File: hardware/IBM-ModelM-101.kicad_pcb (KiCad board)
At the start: 2 copper layers, 150 x 50 mm, 40 parts, among them J1 CONN-61729-USB-B, J2 KEYBOARD_ACTIVE_LINES, J3 KEYBOARD_INPUT_LINES, J4 CHASSIS_GROUND, J5 STATUS_LEDS, J6 DEBUG_FTDI, J7 JTAG, SW1 TACT-TE-FSMSM, SW2 TACT-TE-FSMSM, U1 TLV70233DBV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

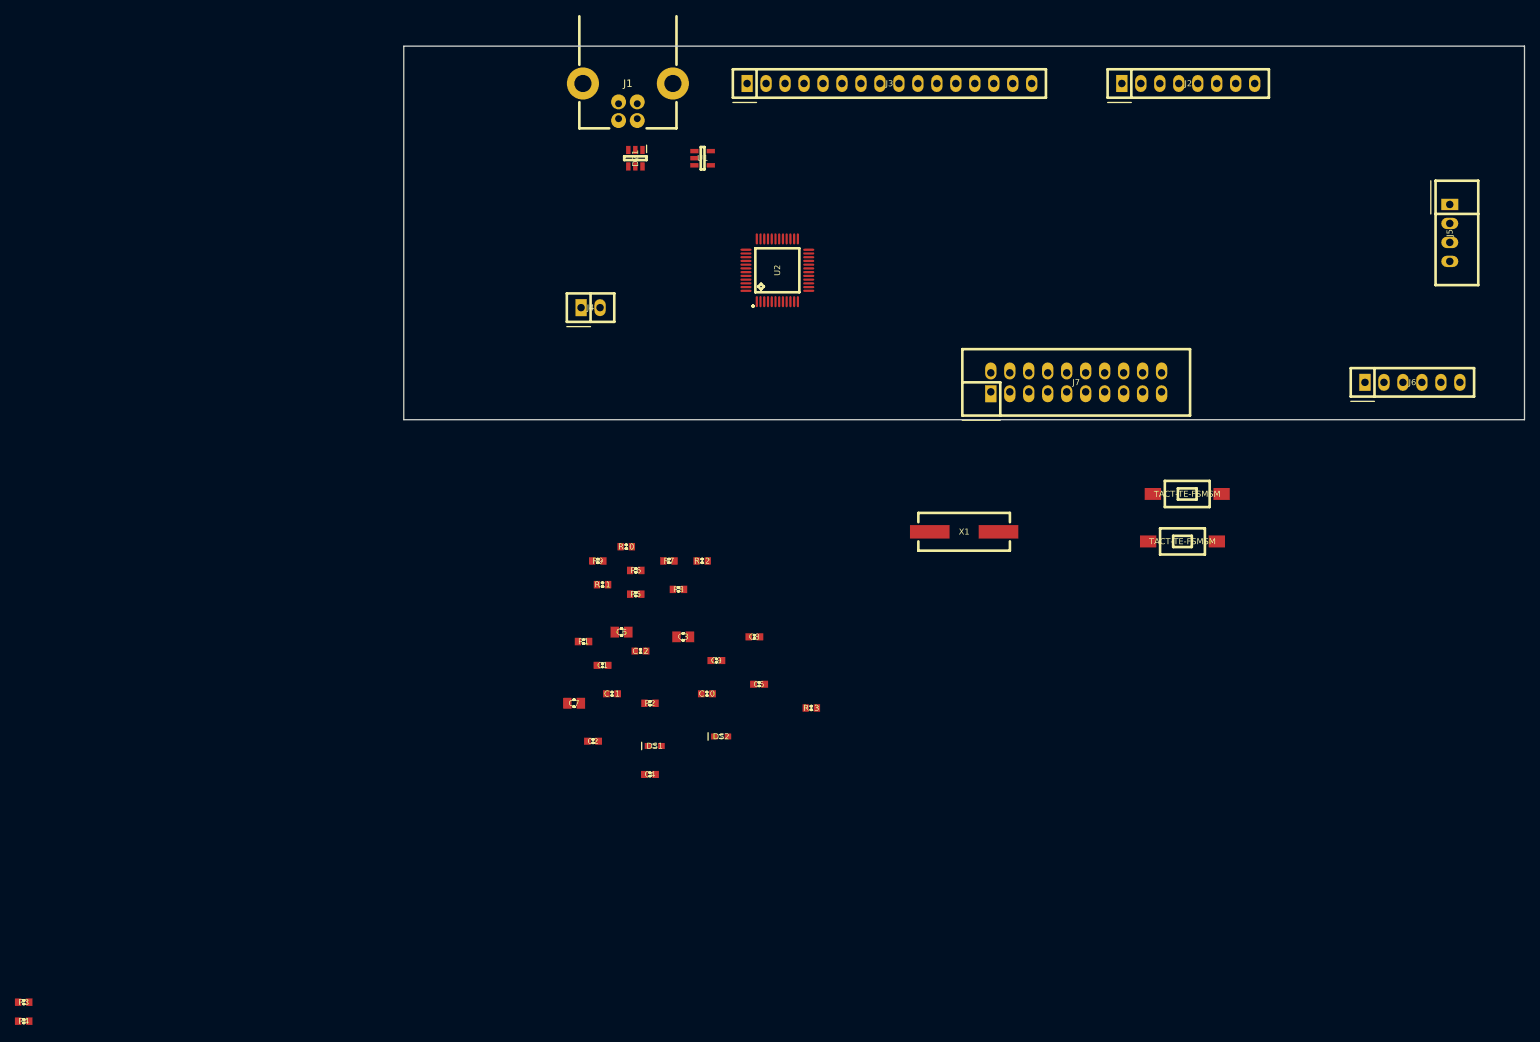
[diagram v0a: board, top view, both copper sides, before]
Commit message: Working on PCB layout
Placement is done. Most of the power, decoupling and support routing
finished.
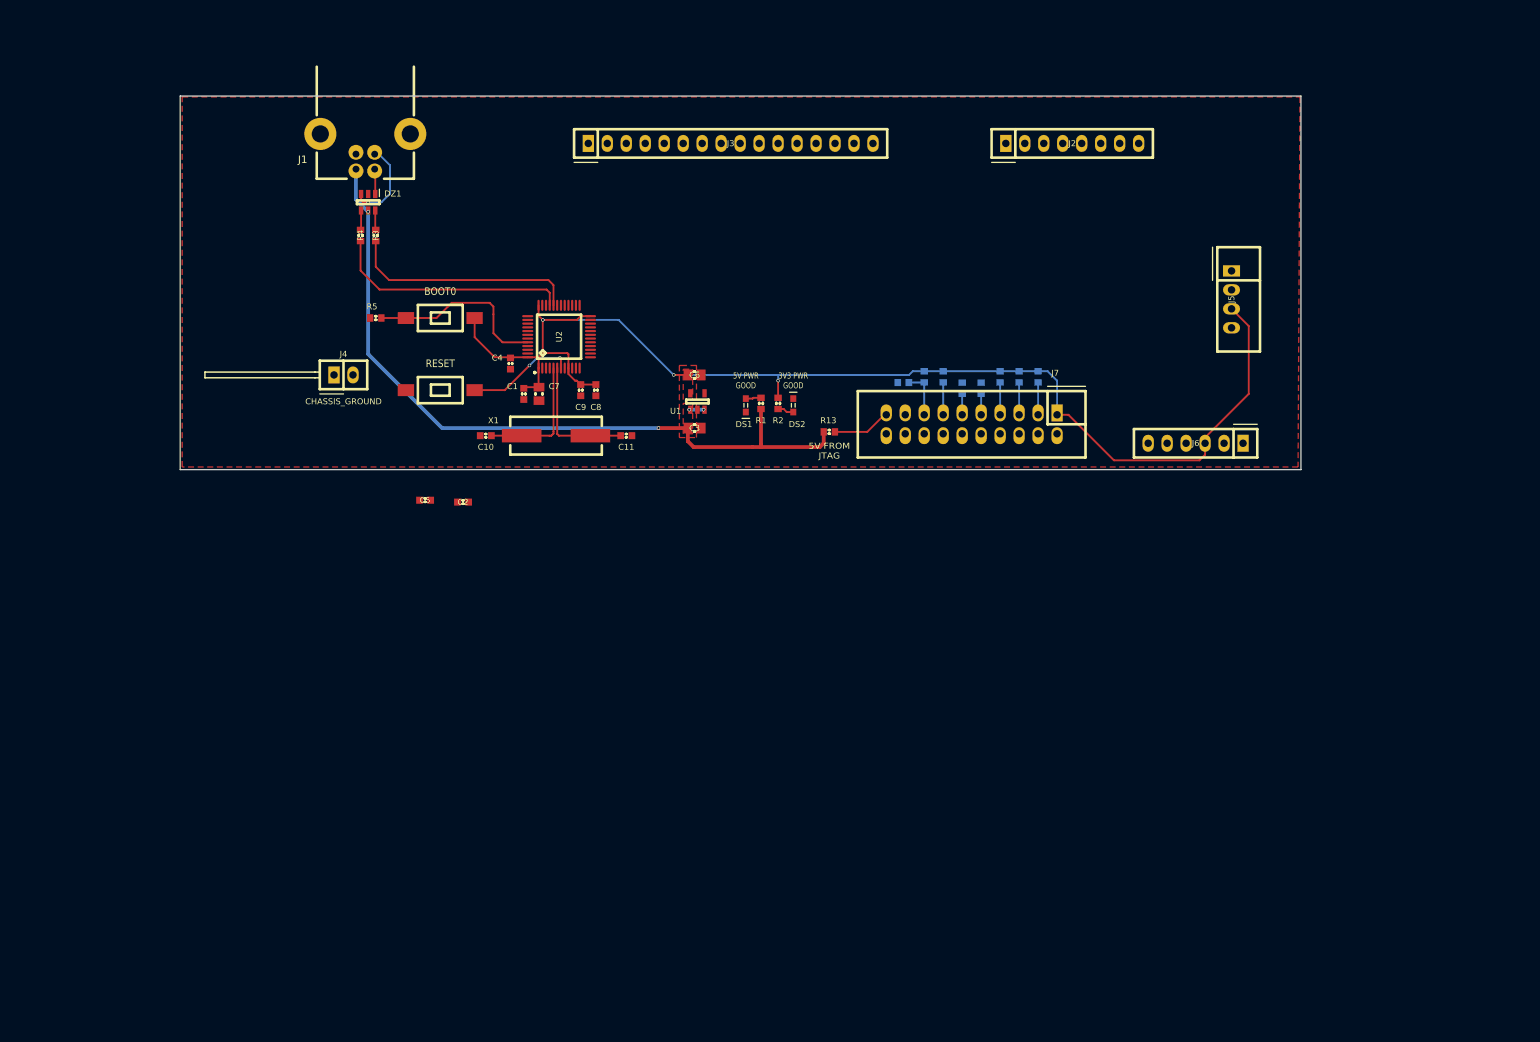
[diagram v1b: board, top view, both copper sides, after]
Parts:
- C12, R10, R11, R12, R6, R7, R8, R9: moved to B.Cu
- C3, C6: value 10uF -> 1uF
- SW1: value TACT-TE-FSMSM -> BOOT0
- SW2: value TACT-TE-FSMSM -> RESET
- moved R4 114.4 mm to (109.2, 45.3), turned to 90 degrees
- moved R3 112.9 mm to (111.3, 45.3), turned to 90 degrees
- moved SW1 102.7 mm to (119.9, 56.4)
- moved SW2 101.4 mm to (119.9, 66.0)
- moved R6 59.8 mm to (199.9, 64.3), turned to 270 degrees
- moved R9 59.2 mm to (194.8, 64.3), turned to 270 degrees
- moved C4 58.1 mm to (129.3, 62.5), turned to 90 degrees
- moved X1 56.1 mm to (135.4, 72.1)
- moved R8 53.7 mm to (197.4, 64.3), turned to 270 degrees
- moved R11 53.4 mm to (187.2, 64.3), turned to 270 degrees
- moved C5 51.0 mm to (117.9, 80.8)
- moved R5 50.8 mm to (111.3, 56.4), turned to 180 degrees
- moved C12 50.3 mm to (181.9, 65.0)
- moved R10 49.7 mm to (189.7, 65.8), turned to 90 degrees
- moved R7 47.8 mm to (192.3, 65.8), turned to 90 degrees
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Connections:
- U1 pad 4: (no net) -> GND
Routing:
- net +3V3: track 0.00 -> 171.1 mm, vias 0 -> 3
- net +5V: track 0.00 -> 102.0 mm, vias 0 -> 4
- net /USB_DP: track 0.00 -> 32.2 mm
- net /USB_DM: track 0.00 -> 31.0 mm
- net /BOOT0: track 0.00 -> 24.7 mm
- net /NRST: track 0.00 -> 21.0 mm, vias 0 -> 2
- net Net-(C11-Pad1): track 0.00 -> 17.4 mm
- net Net-(C10-Pad1): track 0.00 -> 17.2 mm
- net Net-(DZ1-Pad3): track 0.00 -> 11.7 mm, vias 0 -> 1
- net Net-(J7-Pad19): track 0.00 -> 7.82 mm
- net /JTMS/SWDIO: track 0.00 -> 4.33 mm
- net /JTDO: track 0.00 -> 4.33 mm
- net /JTDI: track 0.00 -> 4.33 mm
- net /JNTRST: track 0.00 -> 4.33 mm
- net Net-(DZ1-Pad1): track 0.00 -> 3.37 mm
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- added copper zone on F.Cu, net +3V3
- added copper zone on F.Cu, net +5V
- added copper zone on F.Cu, net GND
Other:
- net class Default: clearance 0.2 -> 0.2032; trace_width 0.25 -> 0.254; via_dia 0.6 -> 0.4572; via_drill 0.4 -> 0.3048
- net class POWER added: clearance 0.254, trace_width 0.508, via_dia 0.4572, via_drill 0.3048
- rule trace_clearance: 0.2 -> 0.2032
- board text added: "3V3 PWR GOOD"
- board text added: "5V FROM JTAG"
- board text added: "5V PWR GOOD"

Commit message: Laying out PCB
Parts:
- U2: moved to B.Cu
- moved J6 65.8 mm to (155.2, 72.9), turned to 0 degrees
- moved SW2 39.2 mm to (93.5, 95.0)
- moved SW1 39.2 mm to (93.0, 84.8)
- moved R5 39.2 mm to (84.3, 84.8)
- moved C4 31.4 mm to (144.5, 89.9)
- moved R1 30.9 mm to (167.9, 98.3)
- moved R13 30.9 mm to (177.0, 102.1)
- moved R2 30.9 mm to (170.2, 98.3)
- moved DS1 30.9 mm to (165.9, 98.6)
- moved DS2 30.9 mm to (172.2, 98.6)
- moved X1 26.5 mm to (121.9, 95.0)
- moved C10 26.5 mm to (112.5, 95.0)
- moved C11 26.5 mm to (131.3, 95.0)
- moved U2 24.4 mm to (158.8, 50.5), turned to 270 degrees
- moved C1 21.0 mm to (138.7, 86.1)
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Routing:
- net +3V3: track 171.1 -> 15.5 mm, vias 3 -> 0
- net +5V: track 102.0 -> 8.49 mm, vias 4 -> 3
- net Net-(J2-Pad8): track 0.00 -> 59.4 mm
- net /JTDO: track 4.33 -> 63.6 mm, vias 0 -> 2
- net Net-(J2-Pad7): track 0.00 -> 57.7 mm
- net Net-(J2-Pad6): track 0.00 -> 56.0 mm
- net Net-(J2-Pad5): track 0.00 -> 54.3 mm
- net Net-(J2-Pad4): track 0.00 -> 52.6 mm
- net Net-(J2-Pad3): track 0.00 -> 51.0 mm
- net Net-(J3-Pad3): track 0.00 -> 49.3 mm, vias 0 -> 2
- net Net-(J2-Pad2): track 0.00 -> 48.9 mm
- net /JTDI: track 4.33 -> 52.5 mm, vias 0 -> 2
- net Net-(J3-Pad2): track 0.00 -> 47.6 mm, vias 0 -> 2
- net Net-(J2-Pad1): track 0.00 -> 46.9 mm
- net Net-(J3-Pad1): track 0.00 -> 46.7 mm, vias 0 -> 2
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
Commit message: Re-working crystal selection and routing.
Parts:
- X1: value 8 MHz -> 8MHz
- moved X1 7.98 mm to (123.2, 102.9)
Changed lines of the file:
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@@
     (links 128)
     (no_connects 61)
-    (area 85.003799 17.363 235.153801 82.423)
+    (area 85.003799 26.605199 235.153801 76.755201)
     (thickness 1.6)
     (drawings 12)
@@
   )
   (module IPC7351-Nominal:XTAL1200X480X460 (layer F.Cu)
-    (at 121.92 94.996)
+    (at 123.19 102.87)
     (descr "Crystal;12.00mm L X 4.80mm W X 4.60mm H")
     (attr smd)
@@
       (effects (font (size 0.8 0.8) (thickness 0.15)))
     )
-    (fp_text value "8 MHz" (at 0 3.556) (layer F.Fab)
-      (effects (font (size 0.8 0.8) (thickness 0.15)))
-    )
+    (fp_text value 8MHz (at 0 3.556) (layer F.Fab)
+      (effects (font (size 0.8 0.8) (thickness 0.15)))
+    )

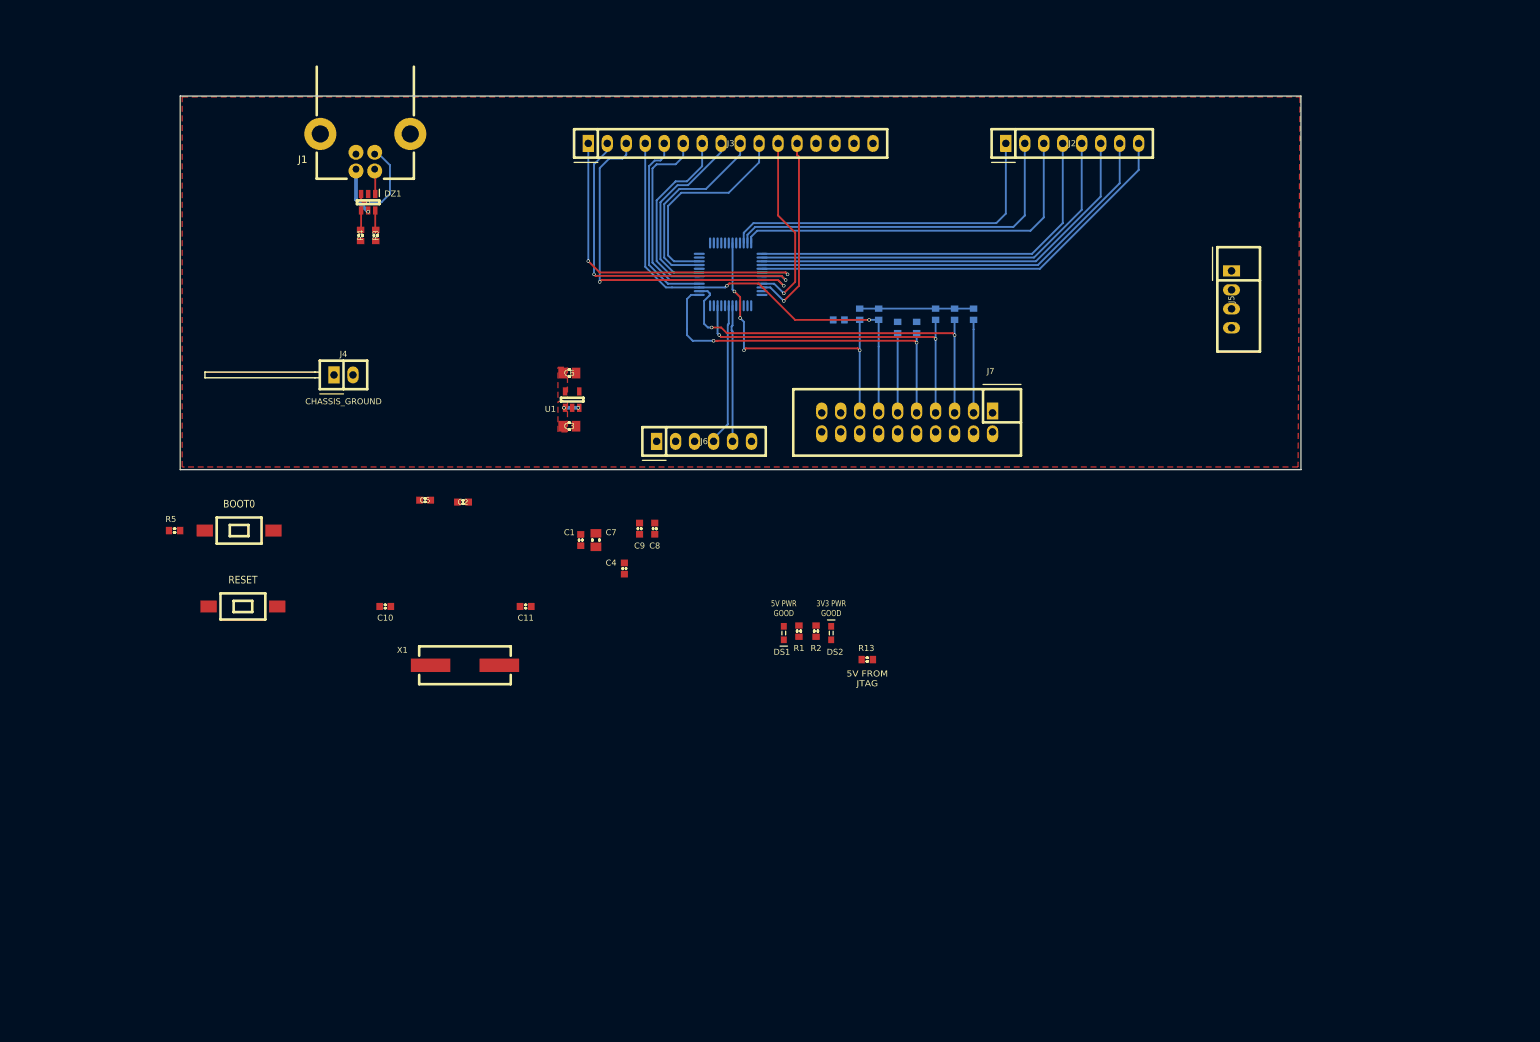
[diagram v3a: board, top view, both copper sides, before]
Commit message: Finished PCB layout
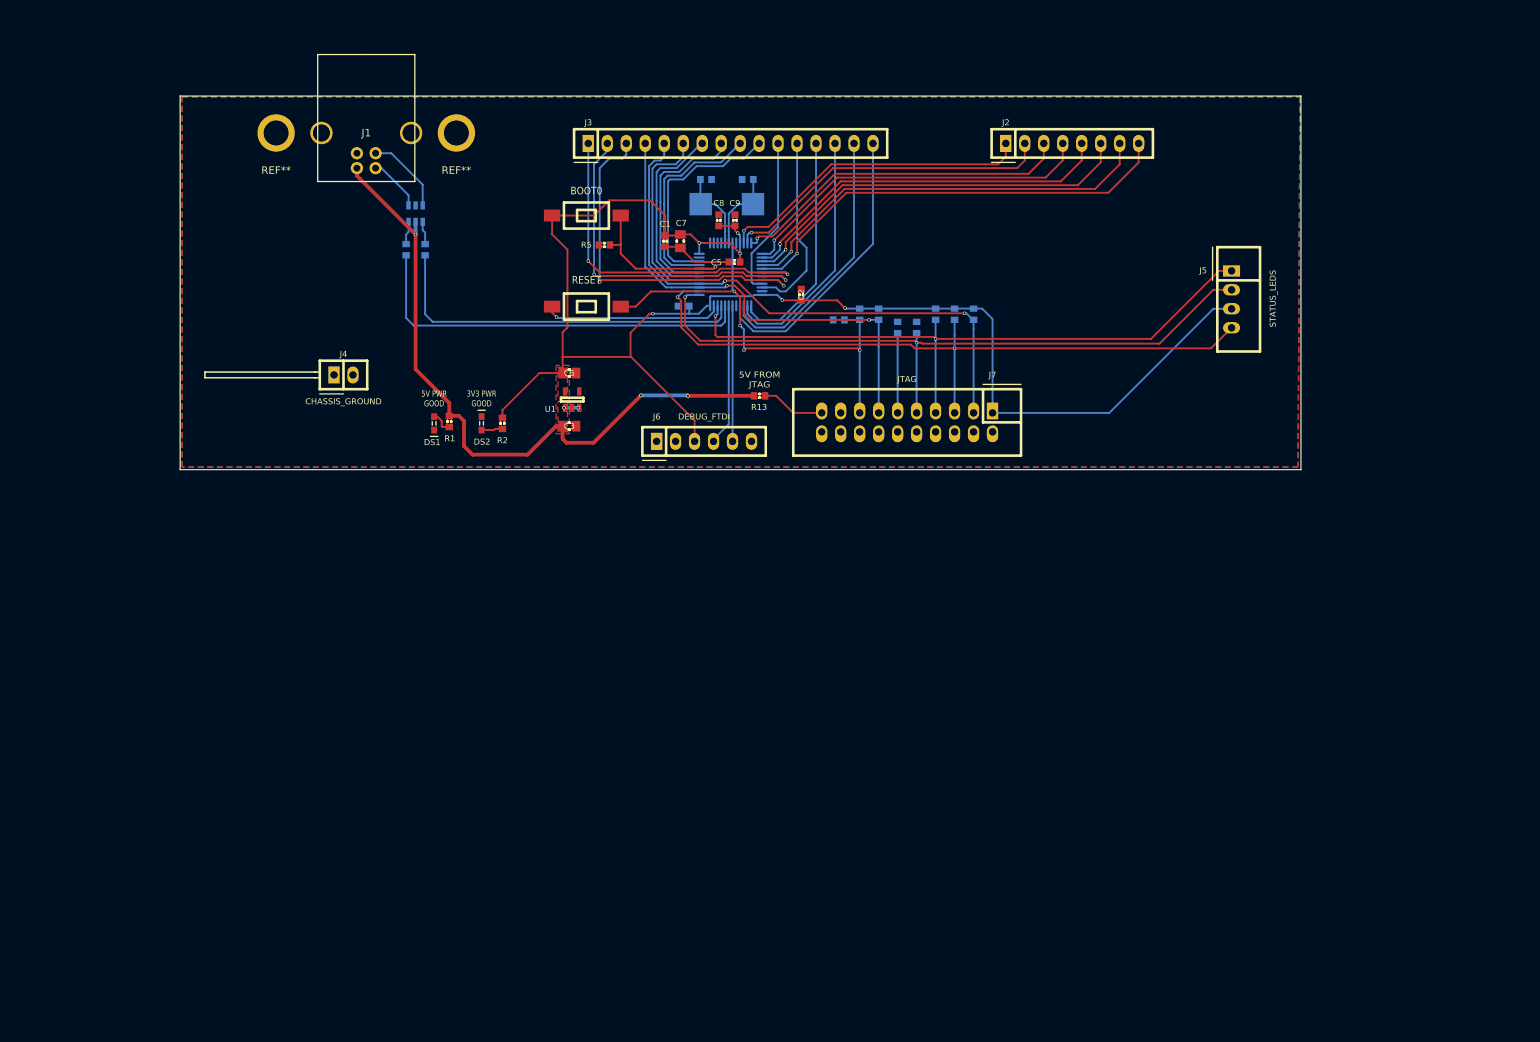
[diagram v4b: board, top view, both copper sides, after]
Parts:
- added REF**: PTH-3MM-PLUS-SUPPORTED, mech:PTH-3MM-PLUS, F.Cu at (122.0, 31.6)
- added REF**: PTH-3MM-PLUS, mech:PTH-3MM-PLUS, F.Cu at (97.9, 31.6)
- C10, C11, C4, DZ1, R3, R4: moved to B.Cu
- J1: value CONN-61729-USB-B -> CONN-MOLEX-0670688000-USB-B; footprint conn-fci:CONN-61729 -> conn-molex:CONN-MOLEX-0670688000-USB_B
- X1: footprint IPC7351-Nominal:XTAL1200X480X460 -> smd-non-ipc:Abracon-ABM2; moved to B.Cu
- moved C10 71.5 mm to (155.4, 37.8), turned to 0 degrees
- moved X1 71.0 mm to (158.2, 41.1)
- moved R5 69.1 mm to (141.9, 46.6)
- moved C11 64.4 mm to (161.0, 37.8), turned to 180 degrees
- moved SW1 62.8 mm to (139.4, 42.7), turned to 180 degrees
- moved SW2 61.0 mm to (139.4, 54.9)
- moved DS1 54.6 mm to (119.1, 70.5)
- moved DS2 54.6 mm to (125.4, 70.5)
- moved R1 54.6 mm to (121.1, 70.2), turned to 270 degrees
- moved C2 53.1 mm to (168.2, 53.3), turned to 270 degrees
- moved C5 52.3 mm to (159.3, 48.9)
- moved R2 50.4 mm to (128.2, 70.5)
- moved C9 43.2 mm to (159.3, 43.3), turned to 270 degrees
- moved C8 42.2 mm to (157.2, 43.3), turned to 270 degrees
- moved C1 41.6 mm to (150.0, 46.1)
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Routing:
- net +3V3: track 15.5 -> 205.6 mm, vias 0 -> 6
- net +5V: track 8.49 -> 93.0 mm, vias 3 -> 5
- net /USB_DM: track 0.00 -> 53.9 mm
- net /USB_DP: track 0.00 -> 49.8 mm
- net /JTCK/SWCLK: track 48.5 -> 93.6 mm
- net /JTMS/SWDIO: track 45.7 -> 89.6 mm
- net /JTDI: track 52.5 -> 95.9 mm
- net /JNTRST: track 37.8 -> 76.8 mm, vias 0 -> 2
- net Net-(J3-Pad16): track 0.00 -> 38.5 mm
- net Net-(J3-Pad15): track 0.00 -> 35.9 mm
- net Net-(J3-Pad14): track 0.00 -> 33.3 mm
- net GND: track 0.00 -> 33.3 mm, vias 0 -> 1
- net Net-(J3-Pad13): track 0.00 -> 30.8 mm
- net /BOOT0: track 0.00 -> 22.6 mm, vias 0 -> 1
- net /NRST: track 45.2 -> 61.3 mm
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- added copper zone on B.Cu, net GND
